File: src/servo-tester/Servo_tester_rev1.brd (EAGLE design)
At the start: 100 x 80 mm, 19 parts, among them IC1 7806T

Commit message: Added pulldown resistors, mounting holes, and text
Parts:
- added R10, R7, R8, R9: 10M, adafruit:0204/5
- moved JP2 45.4 mm to (27.9, 31.8)
- moved D1 32.7 mm to (76.2, 36.8)
- moved R4 32.7 mm to (74.9, 29.2)
- moved R5 32.7 mm to (72.4, 29.2)
- moved R6 32.7 mm to (78.7, 29.2)
- moved JP3 19.1 mm to (50.8, 41.9)
- moved JP5 7.73 mm to (59.7, 29.2)
- moved JP7 6.35 mm to (52.1, 30.5)
- moved JP4 1.27 mm to (64.8, 35.6)
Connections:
- new net S$1: D1.2, JP3.8, U$1.GND
- net GND: no longer D1.2, JP3.8, JP4.2, JP5.2, U$1.GND
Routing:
- net GND: track 240.6 -> 80.5 mm
- net S$1: track 0.00 -> 66.5 mm
- net 6V: track 127.3 -> 78.3 mm
- net LEDR: track 71.4 -> 35.2 mm
- net LEDG: track 66.7 -> 31.8 mm
- net LEDB: track 66.0 -> 31.1 mm
- net SCREEN_DC: track 49.8 -> 30.8 mm
- net SCREEN_RST: track 59.1 -> 40.1 mm
- net SCREEN_CLK: track 39.7 -> 20.6 mm
- net 33V: track 56.0 -> 36.9 mm
- net SCREEN_DATA: track 38.6 -> 19.6 mm
- net SCREEN_CS: track 54.5 -> 35.4 mm
- net BTN2: track 13.8 -> 8.67 mm
- net BTN1: track 14.3 -> 17.9 mm
- net BTN4: track 13.2 -> 9.94 mm
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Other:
- board text added: "Servo Tester v1.0 by Benjamin Russell Western Aero 2020"

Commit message: Fixed discrepancy between brd and sch, corrected pulldowns
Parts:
- moved R9 18.2 mm to (74.9, 43.2), turned to 270 degrees
- moved R5 18.0 mm to (74.9, 11.4)
- moved R6 18.0 mm to (81.3, 11.4)
- moved R4 18.0 mm to (77.5, 11.4)
- moved D1 18.0 mm to (78.7, 19.1)
- moved JP6 16.5 mm to (71.1, 43.2)
- moved JP4 15.9 mm to (78.7, 27.9)
- moved R7 14.9 mm to (81.3, 29.2)
- moved R8 14.0 mm to (76.2, 31.8), turned to 270 degrees
- moved JP5 12.8 mm to (72.4, 30.5)
- moved R10 12.0 mm to (66.0, 34.3), turned to 270 degrees
- moved JP7 12.0 mm to (63.5, 34.3)
- moved JP3 11.4 mm to (50.8, 30.5)
- moved JP2 5.08 mm to (33.0, 31.8)
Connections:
- removed net S$1: D1.2, JP3.8, U$1.GND
- new net 33V_PULLUP: JP3.6, JP4.2, JP5.2, JP6.2, JP7.2
- net BTN1: now also R7.1
- net BTN2: now also R8.2
- net BTN3: now also R9.2
- net BTN4: now also R10.2
- net GND: now also D1.2, JP3.8, R10.1, R7.2, R8.1, R9.1, U$1.GND; no longer JP6.2, JP7.2
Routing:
- net GND: track 80.5 -> 152.0 mm
- net S$1: track 66.5 -> 0.00 mm
- net 33V_PULLUP: track 0.00 -> 42.5 mm
- net SERVO: track 50.5 -> 23.6 mm
- net BTN3: track 15.8 -> 33.0 mm
- net SCREEN_CS: track 35.4 -> 19.7 mm
- net BTN2: track 8.67 -> 24.0 mm
- net LEDR: track 35.2 -> 23.7 mm
- net 33V: track 36.9 -> 25.5 mm
- net SCREEN_RST: track 40.1 -> 28.6 mm
- net SCREEN_DC: track 30.8 -> 19.4 mm
- net SCREEN_DATA: track 19.6 -> 8.15 mm
- net LEDB: track 31.1 -> 20.5 mm
- net BTN4: track 9.94 -> 20.6 mm
- net LEDG: track 31.8 -> 22.5 mm
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
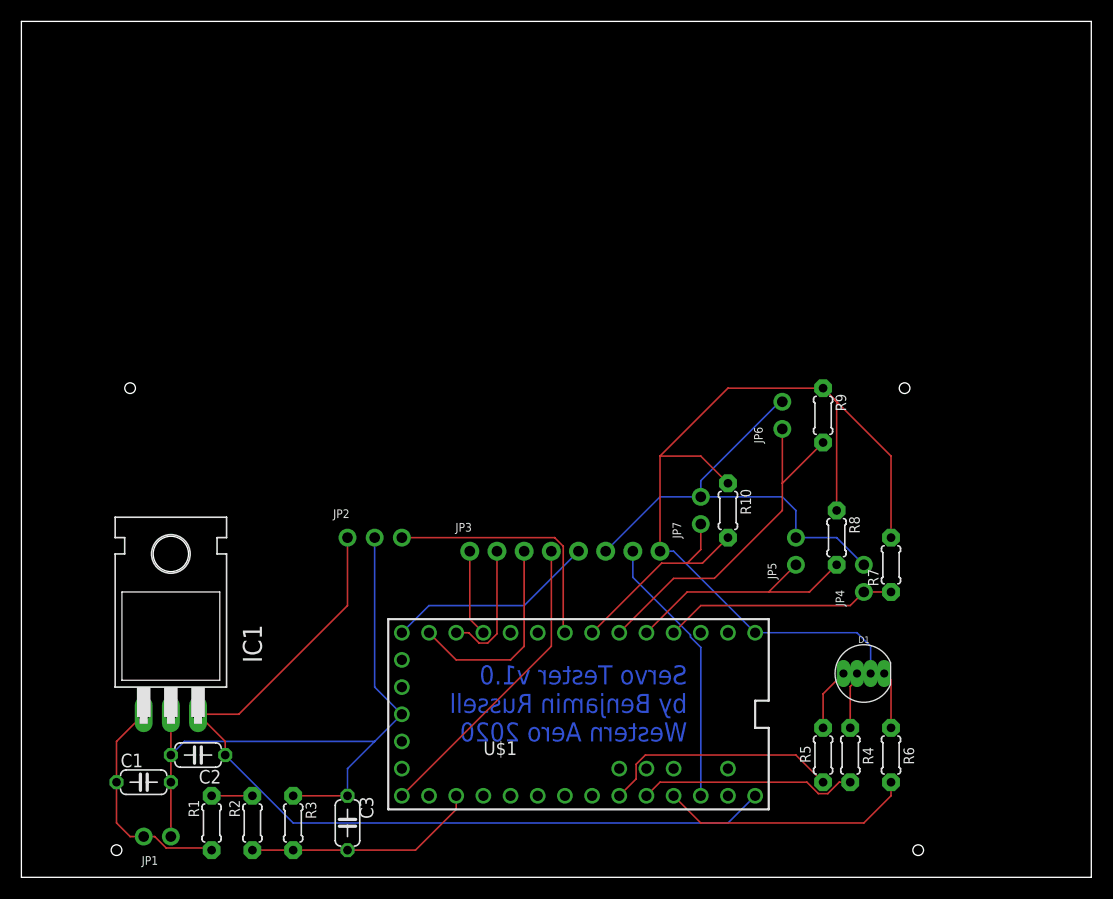
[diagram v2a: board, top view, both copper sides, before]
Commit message: fixed DRCs and made smaller
also added copper fill
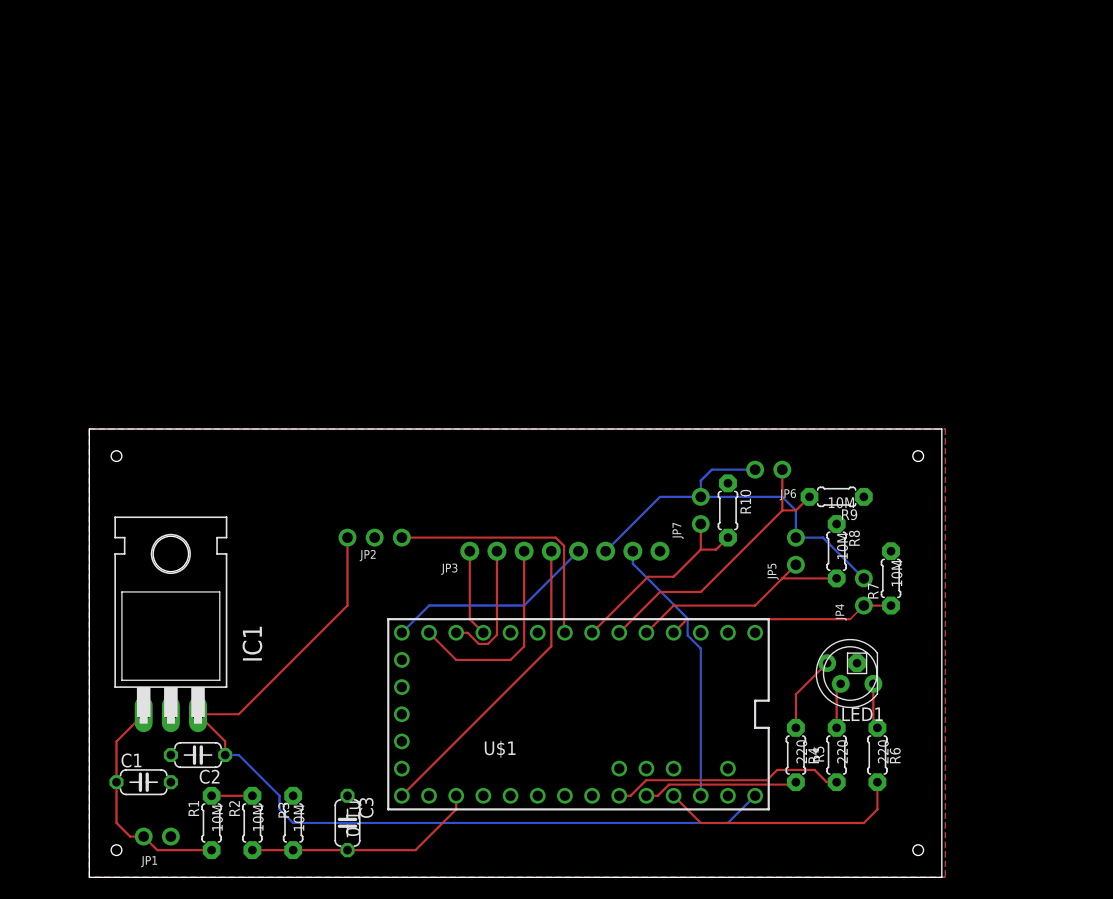
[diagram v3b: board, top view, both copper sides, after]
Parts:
- removed D1: CLEAR, SparkFun-LED:LED-RGB-THRU
- added LED1: RGBLED_CA-5MM, adafruit:LED5MMRGB
- moved R9 7.73 mm to (76.2, 35.6), turned to 180 degrees
- moved JP6 5.24 mm to (69.8, 38.1), turned to 180 degrees
- moved R4 5.08 mm to (72.4, 11.4)
- moved JP4 1.27 mm to (78.7, 26.7)
- moved R7 1.27 mm to (81.3, 27.9)
- moved R8 1.27 mm to (76.2, 30.5)
- moved R5 1.27 mm to (76.2, 11.4)
- moved R6 1.27 mm to (80.0, 11.4)
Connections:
- new net VBAT: U$1.VBAT
- net GND: now also LED1.2; no longer D1.2
- net N$13: now also LED1.1; no longer D1.1
- net N$14: now also LED1.4; no longer D1.3
- net N$15: now also LED1.3; no longer D1.4
- net VIN: no longer U$1.VBAT
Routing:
- net GND: track 152.0 -> 0.00 mm
- net BTN3: track 33.0 -> 26.9 mm
- net LEDB: track 20.5 -> 14.5 mm
- net 33V_PULLUP: track 42.5 -> 37.9 mm
- net BTN2: track 24.0 -> 21.7 mm
- net N$14: track 5.34 -> 7.26 mm
- net BTN4: track 20.6 -> 18.8 mm
- net N$15: track 5.87 -> 4.27 mm
- net N$13: track 5.34 -> 4.27 mm
- net 6V: track 82.6 -> 83.3 mm
- net LEDG: track 22.5 -> 21.8 mm
- net BTN1: track 21.9 -> 21.4 mm
- net LEDR: track 23.7 -> 23.2 mm
- added copper zone on layer 1, net GND
- added copper zone on layer 16, net GND
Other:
- board size 100 x 80 mm -> 79.7 x 41.9 mm
